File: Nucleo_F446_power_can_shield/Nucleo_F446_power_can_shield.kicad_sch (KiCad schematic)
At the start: 31 parts, among them J1 ISOCAN1, J10 ISOCAN2, J11 CAN1, J12 CAN2, J13 ISOCAN1, J14 ISOCAN2, J15 CAN1, J16 CAN2, J17 RJ45, J18 RJ45, J19 I2C3, J2 ISOCAN2, J20 UART4, J21 xt60 male, J3 CAN1, J4 CAN2, J5 ISOCAN1, J6 ISOCAN2, J7 CAN1, J8 CAN2, J9 ISOCAN1, M1 Isolated-Can-Transceiver-Modu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, M2 Isolated-Can-Transceiver-Modu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, M3 TJA1050_Module, M4 TJA1050_Module, U1 NUCLEO-F446RE, U2 MP1584

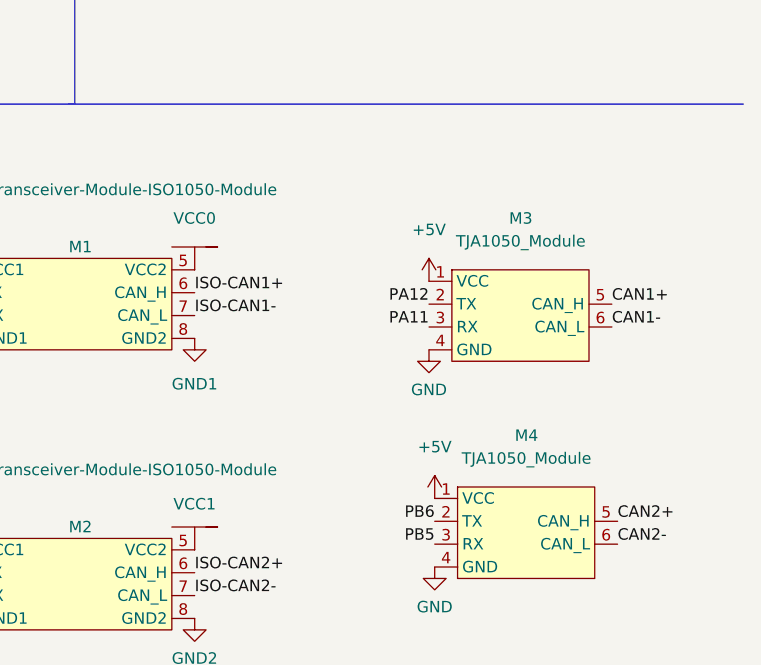
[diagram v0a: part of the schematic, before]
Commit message: add bullyU
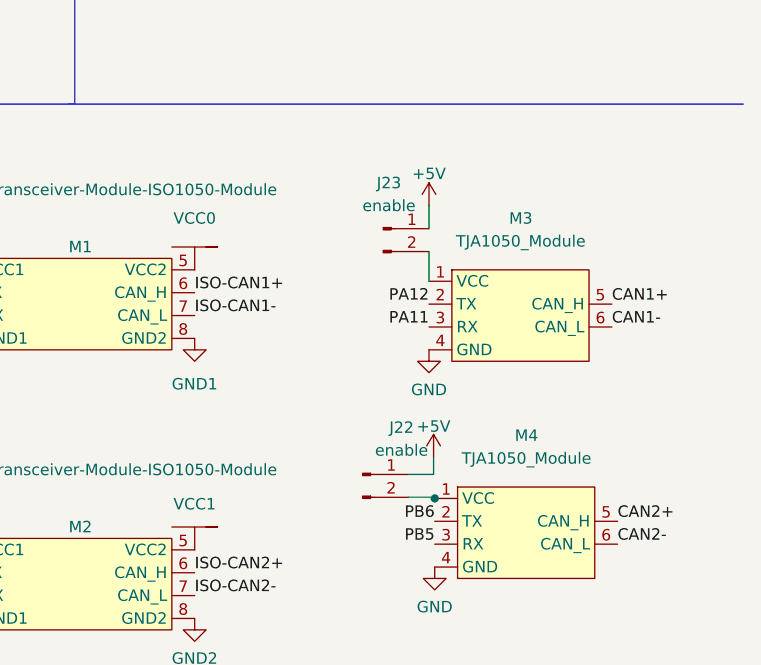
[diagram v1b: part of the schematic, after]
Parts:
- added J22, J23: enable, Connector_PinHeader_2.54mm:PinHeader_1x02_P2.54mm_Vertical, symbol Connector:Conn_01x02_Male
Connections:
- net +5V: now also J22.1 (Pin_1), J23.1 (Pin_1); no longer M3.1 (VCC), M4.1 (VCC)
- new net: J23.2 (Pin_2), M3.1 (VCC)
- new net: J22.2 (Pin_2), M4.1 (VCC)
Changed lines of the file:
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@@
   (junction (at 162.56 140.97) (diameter 0) (color 0 0 0 0)
+  )
+  (junction (at 250.19 141.605) (diameter 0) (color 0 0 0 0)
   )
   (junction (at 226.06 50.8) (diameter 0) (color 0 0 0 0)
@@
   (no_connect (at 67.945 152.4))
   (no_connect (at 132.08 139.7))
+  (wire (pts (xy 247.269 141.478) (xy 250.19 141.478))
+    (stroke (width 0) (type default) (color 0 0 0 0))
+  )
   (wire (pts (xy 169.545 171.45) (xy 169.545 173.355))
     (stroke (width 0) (type default) (color 0 0 0 0))
@@
     (stroke (width 0) (type default) (color 0 0 0 0))
   )
+  (wire (pts (xy 249.555 109.093) (xy 249.555 111.633))
+    (stroke (width 0) (type default) (color 0 0 0 0))
+  )
   (wire (pts (xy 162.56 138.43) (xy 162.56 135.255))
     (stroke (width 0) (type default) (color 0 0 0 0))
@@
     (stroke (width 0) (type default) (color 0 0 0 0))
   )
+  (wire (pts (xy 250.063 137.033) (xy 250.063 138.938))
+    (stroke (width 0) (type default) (color 0 0 0 0))
+  )
   (wire (pts (xy 226.06 49.53) (xy 226.06 50.8))
     (stroke (width 0) (type default) (color 0 0 0 0))
@@
     (stroke (width 0) (type default) (color 0 0 0 0))
   )
+  (wire (pts (xy 250.19 141.478) (xy 250.19 141.605))
+    (stroke (width 0) (type default) (color 0 0 0 0))
+  )
   (wire (pts (xy 69.088 47.752) (xy 69.088 45.974))
     (stroke (width 0) (type default) (color 0 0 0 0))
@@
     (stroke (width 0) (type default) (color 0 0 0 0))
   )
+  (wire (pts (xy 249.555 114.173) (xy 249.555 117.475))
+    (stroke (width 0) (type default) (color 0 0 0 0))
+  )
   (wire (pts (xy 162.56 140.97) (xy 166.37 140.97))
     (stroke (width 0) (type default) (color 0 0 0 0))
@@
     (stroke (width 0) (type default) (color 0 0 0 0))
   )
+  (wire (pts (xy 247.269 138.938) (xy 250.063 138.938))
+    (stroke (width 0) (type default) (color 0 0 0 0))
+  )
   (polyline (pts (xy 210.185 12.065) (xy 210.185 97.79))
     (stroke (width 0) (type default) (color 0 0 0 0))
@@
   (label "ISO-CAN2-" (at 223.52 152.4 0)
     (effects (font (size 1.27 1.27)) (justify left bottom))
+  )
+  (symbol (lib_id "Connector:Conn_01x02_Male") (at 244.475 111.633 0) (unit 1)
+    (in_bom yes) (on_board yes) (fields_autoplaced)
+    (property "Reference" "J23" (id 0) (at 245.11 106.553 0))
+    (property "Value" "enable" (id 1) (at 245.11 109.093 0))
+    (property "Footprint" "Connector_PinHeader_2.54mm:PinHeader_1x02_P2.54mm_Vertical" (id 2) (at 244.475 111.633 0)
+      (effects (font (size 1.27 1.27)) hide)
+    )
+    (property "Datasheet" "~" (id 3) (at 244.475 111.633 0)
+      (effects (font (size 1.27 1.27)) hide)
+    )
+    (pin "1")
+    (pin "2")
   )
   (symbol (lib_id "PolyuRobotics:VCC1") (at 163.83 167.005 0) (unit 1)
@@
     (pin "1")
   )
-  (symbol (lib_id "power:+5V") (at 249.555 117.475 0) (unit 1)
-    (in_bom yes) (on_board yes) (fields_autoplaced)
-    (property "Reference" "#PWR0105" (id 0) (at 249.555 121.285 0)
-      (effects (font (size 1.27 1.27)) hide)
-    )
-    (property "Value" "+5V" (id 1) (at 249.555 111.76 0))
-    (property "Footprint" "" (id 2) (at 249.555 117.475 0)
-      (effects (font (size 1.27 1.27)) hide)
-    )
-    (property "Datasheet" "" (id 3) (at 249.555 117.475 0)
+  (symbol (lib_id "power:+5V") (at 249.555 109.093 0) (unit 1)
+    (in_bom yes) (on_board yes)
+    (property "Reference" "#PWR0105" (id 0) (at 249.555 112.903 0)
+      (effects (font (size 1.27 1.27)) hide)
+    )
+    (property "Value" "+5V" (id 1) (at 249.555 105.537 0))
+    (property "Footprint" "" (id 2) (at 249.555 109.093 0)
+      (effects (font (size 1.27 1.27)) hide)
+    )
+    (property "Datasheet" "" (id 3) (at 249.555 109.093 0)
       (effects (font (size 1.27 1.27)) hide)
     )
@@
     (pin "1")
   )
-  (symbol (lib_id "power:+5V") (at 250.19 141.605 0) (unit 1)
-    (in_bom yes) (on_board yes) (fields_autoplaced)
-    (property "Reference" "#PWR0112" (id 0) (at 250.19 145.415 0)
-      (effects (font (size 1.27 1.27)) hide)
-    )
-    (property "Value" "+5V" (id 1) (at 250.19 135.89 0))
-    (property "Footprint" "" (id 2) (at 250.19 141.605 0)
-      (effects (font (size 1.27 1.27)) hide)
-    )
-    (property "Datasheet" "" (id 3) (at 250.19 141.605 0)
+  (symbol (lib_id "power:+5V") (at 250.063 137.033 0) (unit 1)
+    (in_bom yes) (on_board yes)
+    (property "Reference" "#PWR0112" (id 0) (at 250.063 140.843 0)
+      (effects (font (size 1.27 1.27)) hide)
+    )
+    (property "Value" "+5V" (id 1) (at 250.063 133.604 0))
+    (property "Footprint" "" (id 2) (at 250.063 137.033 0)
+      (effects (font (size 1.27 1.27)) hide)
+    )
+    (property "Datasheet" "" (id 3) (at 250.063 137.033 0)
       (effects (font (size 1.27 1.27)) hide)
     )
@@
     )
     (pin "")
+  )
+  (symbol (lib_id "Connector:Conn_01x02_Male") (at 242.189 138.938 0) (unit 1)
+    (in_bom yes) (on_board yes)
+    (property "Reference" "J22" (id 0) (at 246.507 133.731 0))
+    (property "Value" "enable" (id 1) (at 246.507 136.271 0))
+    (property "Footprint" "Connector_PinHeader_2.54mm:PinHeader_1x02_P2.54mm_Vertical" (id 2) (at 242.189 138.938 0)
+      (effects (font (size 1.27 1.27)) hide)
+    )
+    (property "Datasheet" "~" (id 3) (at 242.189 138.938 0)
+      (effects (font (size 1.27 1.27)) hide)
+    )
+    (pin "1")
+    (pin "2")
   )
   (symbol (lib_id "PolyuRobotics:MP1584") (at 243.332 53.34 0) (unit 1)
@@
       (reference "J21") (unit 1) (value "xt60 male") (footprint "PolyuRobotics:XT60PW-M20")
     )
+    (path "/ecfc14dc-44a0-494b-bb59-728399d8e8f3"
+      (reference "J22") (unit 1) (value "enable") (footprint "Connector_PinHeader_2.54mm:PinHeader_1x02_P2.54mm_Vertical")
+    )
+    (path "/02faaa9a-5b8a-455b-a497-72dbb04f0ead"
+      (reference "J23") (unit 1) (value "enable") (footprint "Connector_PinHeader_2.54mm:PinHeader_1x02_P2.54mm_Vertical")
+    )
     (path "/fc93b073-c298-4ddf-a4a1-4e1430dd42f6"

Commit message: oh
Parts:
- added D1, D2, D4, D5: can_led, LED_SMD:LED_0805_2012Metric_Pad1.15x1.40mm_HandSolder, symbol Device:LED_Small
- added D3: power_led, LED_SMD:LED_0805_2012Metric_Pad1.15x1.40mm_HandSolder, symbol Device:LED_Small
- added J24, J25: enable, Connector_PinHeader_2.54mm:PinHeader_1x02_P2.54mm_Vertical, symbol Connector:Conn_01x02_Male
- added R1, R2, R3, R4, R5: 10K, Resistor_SMD:R_0805_2012Metric_Pad1.20x1.40mm_HandSolder, symbol Device:R_Small
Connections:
- net +5V: now also J24.1 (Pin_1), J25.1 (Pin_1), R3.1; no longer M1.1 (VCC1), M2.1 (VCC1)
- net GND: now also D1.1 (K), D2.1 (K), D3.1 (K), D4.1 (K), D5.1 (K)
- net at J23.2 (Pin_2), M3.1 (VCC): now also R4.1
- net at J22.2 (Pin_2), M4.1 (VCC): now also R5.1
- new net: D5.2 (A), R5.2
- new net: D2.2 (A), R2.2
- new net: D4.2 (A), R4.2
- new net: D3.2 (A), R3.2
- new net: J25.2 (Pin_2), M2.1 (VCC1), R2.1
- new net: J24.2 (Pin_2), M1.1 (VCC1), R1.1
- new net: D1.2 (A), R1.2
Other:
- moved on the sheet: J22, J23, M1, M2, M3, M4

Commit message: diode
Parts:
- added D6: ss24, Diode_SMD:D_SMB-SMC_Universal_Handsoldering, symbol Device:D_Schottky
- added D7: SMBJ24CA, Diode_SMD:D_SMB-SMC_Universal_Handsoldering, symbol Device:D_Schottky
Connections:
- net +24V: now also D6.2 (A), D7.1 (K); no longer C3.1, U2.IN1+ (VIN+), U2.IN2+ (VIN+)
- net GND: now also D7.2 (A)
- new net: C3.1, D6.1 (K), U2.IN1+ (VIN+), U2.IN2+ (VIN+)
- no-connect marks 70 -> 71
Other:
- moved on the sheet: C4, J21

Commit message: add diode
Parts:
- added D8: SMBJ9VCA, Diode_SMD:D_SMB-SMC_Universal_Handsoldering, symbol Device:D_Schottky
- added R6, R7: 4.7k, Resistor_SMD:R_0805_2012Metric_Pad1.20x1.40mm_HandSolder, symbol Device:R_Small
- R3: value 10K -> 22K
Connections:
- net +3V3: now also R6.1, R7.1
- net +5V: no longer R3.1
- net GND: now also D8.2 (A)
- net PA8: now also R6.2
- net PB4: now also R7.2
- net VCC: now also R3.1, D8.1 (K)
- no-connect marks 71 -> 72
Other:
- moved on the sheet: D3, J19, J20, R3

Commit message: gerber
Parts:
- D6, D7, D8: footprint Diode_SMD:D_SMB-SMC_Universal_Handsoldering -> Diode_SMD:D_SMB_Handsoldering
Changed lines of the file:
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@@
     (property "Reference" "D6" (id 0) (at 219.7735 44.45 0))
     (property "Value" "ss24" (id 1) (at 219.7735 46.99 0))
-    (property "Footprint" "Diode_SMD:D_SMB-SMC_Universal_Handsoldering" (id 2) (at 219.456 50.8 0)
+    (property "Footprint" "Diode_SMD:D_SMB_Handsoldering" (id 2) (at 219.456 50.8 0)
       (effects (font (size 1.27 1.27)) hide)
     )
@@
       (effects (font (size 1.27 1.27)) (justify left))
     )
-    (property "Footprint" "Diode_SMD:D_SMB-SMC_Universal_Handsoldering" (id 2) (at 237.49 77.47 0)
+    (property "Footprint" "Diode_SMD:D_SMB_Handsoldering" (id 2) (at 237.49 77.47 0)
       (effects (font (size 1.27 1.27)) hide)
     )
@@
       (effects (font (size 1.27 1.27)) (justify left))
     )
-    (property "Footprint" "Diode_SMD:D_SMB-SMC_Universal_Handsoldering" (id 2) (at 230.505 29.845 0)
+    (property "Footprint" "Diode_SMD:D_SMB_Handsoldering" (id 2) (at 230.505 29.845 0)
       (effects (font (size 1.27 1.27)) hide)
     )
@@
     )
     (path "/2e591c2a-ca64-4531-bdf1-e4476f71d798"
-      (reference "D6") (unit 1) (value "ss24") (footprint "Diode_SMD:D_SMB-SMC_Universal_Handsoldering")
+      (reference "D6") (unit 1) (value "ss24") (footprint "Diode_SMD:D_SMB_Handsoldering")
     )
     (path "/a59125f3-ac20-46be-a7ff-41c20858c454"
-      (reference "D7") (unit 1) (value "SMBJ24CA") (footprint "Diode_SMD:D_SMB-SMC_Universal_Handsoldering")
+      (reference "D7") (unit 1) (value "SMBJ24CA") (footprint "Diode_SMD:D_SMB_Handsoldering")
     )
     (path "/896f4657-f42f-4d04-aefd-2a0b33a5b453"
-      (reference "D8") (unit 1) (value "SMBJ9VCA") (footprint "Diode_SMD:D_SMB-SMC_Universal_Handsoldering")
+      (reference "D8") (unit 1) (value "SMBJ9VCA") (footprint "Diode_SMD:D_SMB_Handsoldering")
     )
     (path "/7da26a16-756d-42bb-b6f2-401c9b58e7f5"
